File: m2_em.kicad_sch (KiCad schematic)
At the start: 26 parts, among them J15 Bus_M.2_Socket_M, J81 Bus_M.2_Socket_E

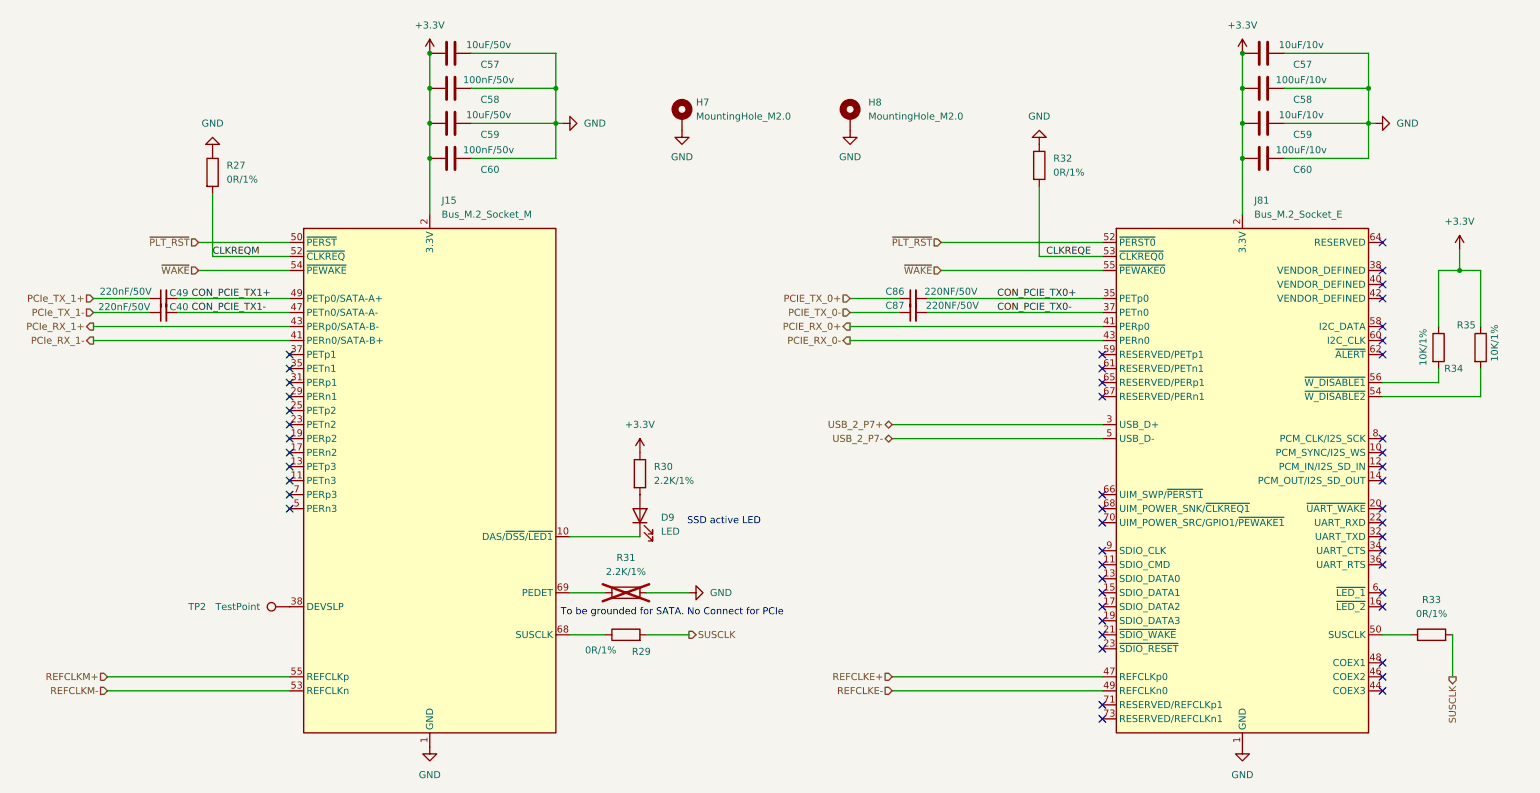
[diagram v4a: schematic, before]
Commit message: Fixed annotation errors duplicate designators on passive components R11 and J15 so that schematic could be imported into pcb. There might be some missing footprints... starting that investigation
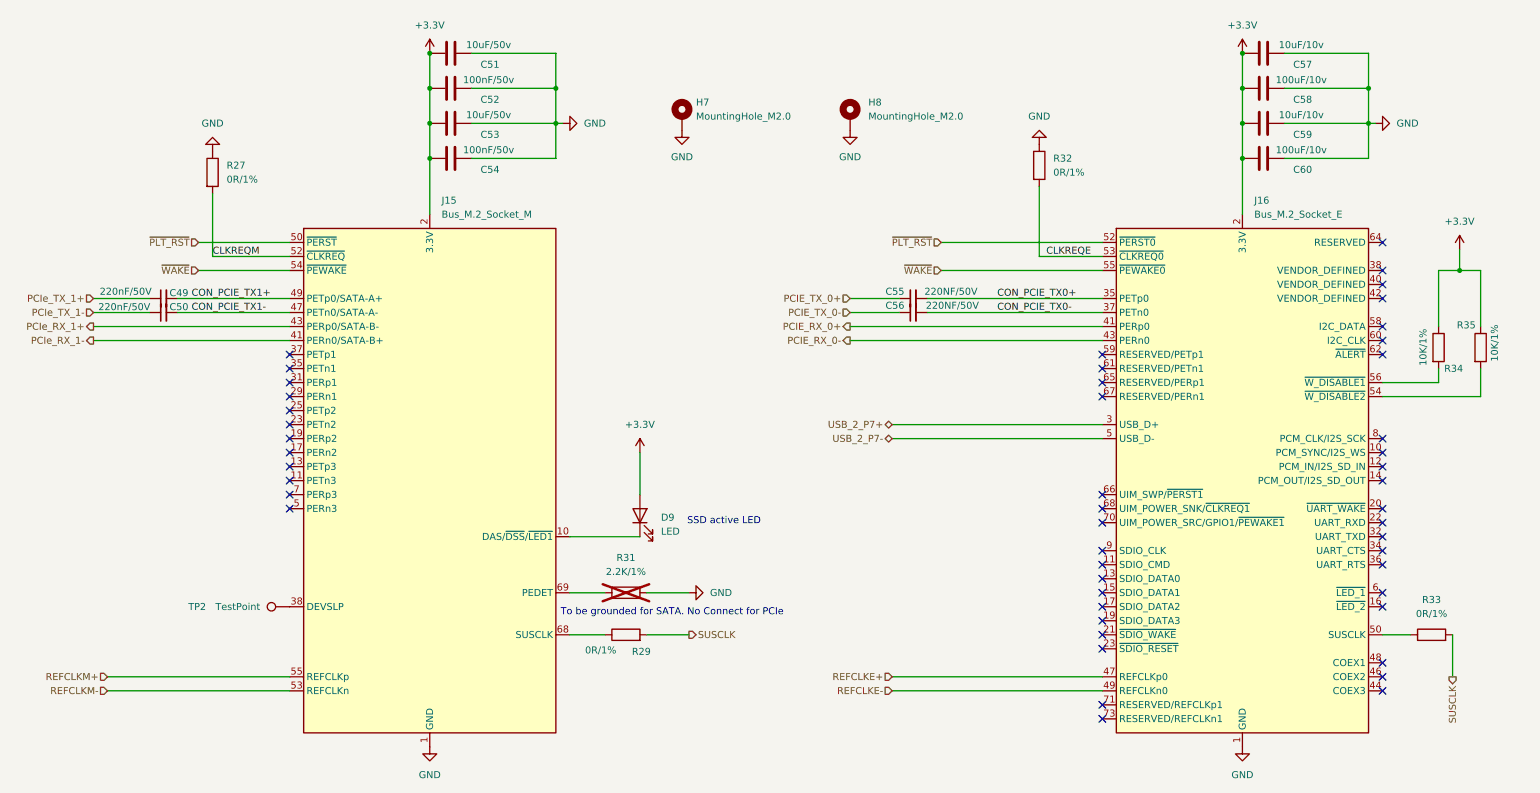
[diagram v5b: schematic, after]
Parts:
- removed R30: 2.2K/1%, A_HDJ_Library:R_0402_1005Metric, symbol Device:R
- renumbered C40 to C50, C57 to C51, C58 to C52, C59 to C53, C60 to C54, C86 to C55, C87 to C56, J81 to J16
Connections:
- net +3.3V: now also D9.2 (A)
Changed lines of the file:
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@@
+	(wire
+		(pts
+			(xy 124.46 102.87) (xy 124.46 110.49)
+		)
+		(stroke
+			(width 0)
+			(type default)
+		)
+	)
 	(wire
 		(pts
@@
 		(in_pos_files yes)
 		(dnp no)
-		(property "Reference" "C40"
+		(property "Reference" "C50"
 			(at 40.894 76.454 90)
 			(show_name no)
@@
 			(project "Carrier_Board"
 				(path "/e768274e-12f3-4f83-96f6-abb7638e0bc1/c9d591b5-2734-4735-842a-ee158b52d7b9"
-					(reference "C40")
+					(reference "C50")
 					(unit 1)
 				)
@@
 	)
 	(symbol
-		(lib_id "Device:R")
-		(at 124.46 106.68 0)
-		(unit 1)
-		(body_style 1)
-		(exclude_from_sim no)
-		(in_bom yes)
-		(on_board yes)
-		(in_pos_files yes)
-		(dnp no)
-		(fields_autoplaced yes)
-		(property "Reference" "R30"
-			(at 127 105.4099 0)
-			(show_name no)
-			(do_not_autoplace no)
-			(effects
-				(font
-					(size 1.27 1.27)
-				)
-				(justify left)
-			)
-		)
-		(property "Value" "2.2K/1%"
-			(at 127 107.9499 0)
-			(show_name no)
-			(do_not_autoplace no)
-			(effects
-				(font
-					(size 1.27 1.27)
-				)
-				(justify left)
-			)
-		)
-		(property "Footprint" "A_HDJ_Library:R_0402_1005Metric"
-			(at 122.682 106.68 90)
-			(hide yes)
-			(show_name no)
-			(do_not_autoplace no)
-			(effects
-				(font
-					(size 1.27 1.27)
-				)
-			)
-		)
-		(property "Datasheet" ""
-			(at 124.46 106.68 0)
-			(hide yes)
-			(show_name no)
-			(do_not_autoplace no)
-			(effects
-				(font
-					(size 1.27 1.27)
-				)
-			)
-		)
-		(property "Description" "Resistor"
-			(at 124.46 106.68 0)
-			(hide yes)
-			(show_name no)
-			(do_not_autoplace no)
-			(effects
-				(font
-					(size 1.27 1.27)
-				)
-			)
-		)
-		(property "Purpose" ""
-			(at 124.46 106.68 0)
-			(show_name no)
-			(do_not_autoplace no)
-			(effects
-				(font
-					(size 1.27 1.27)
-				)
-			)
-		)
-		(pin "1"
-		)
-		(pin "2"
-		)
-		(instances
-			(project "Carrier_Board"
-				(path "/e768274e-12f3-4f83-96f6-abb7638e0bc1/c9d591b5-2734-4735-842a-ee158b52d7b9"
-					(reference "R30")
-					(unit 1)
-				)
-			)
-		)
-	)
-	(symbol
 		(lib_id "Device:C")
 		(at 90.17 36.83 90)
@@
 		(in_pos_files yes)
 		(dnp no)
-		(property "Reference" "C58"
+		(property "Reference" "C52"
 			(at 97.282 38.862 90)
 			(show_name no)
@@
 			(project "Carrier_Board"
 				(path "/e768274e-12f3-4f83-96f6-abb7638e0bc1/c9d591b5-2734-4735-842a-ee158b52d7b9"
-					(reference "C58")
+					(reference "C52")
 					(unit 1)
 				)
@@
 		(in_pos_files yes)
 		(dnp no)
-		(property "Reference" "C87"
+		(property "Reference" "C56"
 			(at 170.688 76.2 90)
 			(show_name no)
@@
 			(project "Carrier_Board"
 				(path "/e768274e-12f3-4f83-96f6-abb7638e0bc1/c9d591b5-2734-4735-842a-ee158b52d7b9"
-					(reference "C87")
+					(reference "C56")
 					(unit 1)
 				)
@@
 		(in_pos_files yes)
 		(dnp no)
-		(property "Reference" "C60"
+		(property "Reference" "C54"
 			(at 97.282 51.562 90)
 			(show_name no)
@@
 			(project "Carrier_Board"
 				(path "/e768274e-12f3-4f83-96f6-abb7638e0bc1/c9d591b5-2734-4735-842a-ee158b52d7b9"
-					(reference "C60")
+					(reference "C54")
 					(unit 1)
 				)
@@
 		(in_pos_files yes)
 		(dnp no)
-		(property "Reference" "C59"
+		(property "Reference" "C53"
 			(at 97.282 45.212 90)
 			(show_name no)
@@
 			(project "Carrier_Board"
 				(path "/e768274e-12f3-4f83-96f6-abb7638e0bc1/c9d591b5-2734-4735-842a-ee158b52d7b9"
-					(reference "C59")
+					(reference "C53")
 					(unit 1)
 				)
@@
 		(dnp no)
 		(fields_autoplaced yes)
-		(property "Reference" "J81"
+		(property "Reference" "J16"
 			(at 235.8233 57.15 0)
 			(show_name no)
@@
 			(project "Carrier_Board"
 				(path "/e768274e-12f3-4f83-96f6-abb7638e0bc1/c9d591b5-2734-4735-842a-ee158b52d7b9"
-					(reference "J81")
+					(reference "J16")
 					(unit 1)
 				)
@@
 		(in_pos_files yes)
 		(dnp no)
-		(property "Reference" "C57"
+		(property "Reference" "C51"
 			(at 97.282 32.512 90)
 			(show_name no)
@@
 			(project "Carrier_Board"
 				(path "/e768274e-12f3-4f83-96f6-abb7638e0bc1/c9d591b5-2734-4735-842a-ee158b52d7b9"
-					(reference "C57")
+					(reference "C51")
 					(unit 1)
 				)
@@
 		(in_pos_files yes)
 		(dnp no)
-		(property "Reference" "C86"
+		(property "Reference" "C55"
 			(at 170.688 73.66 90)
 			(show_name no)
@@
 			(project "Carrier_Board"
 				(path "/e768274e-12f3-4f83-96f6-abb7638e0bc1/c9d591b5-2734-4735-842a-ee158b52d7b9"
-					(reference "C86")
+					(reference "C55")
 					(unit 1)
 				)

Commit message: Updated all the footprints into the pcb editor but all the designator numbers have changed... I have tp go back and fix each one
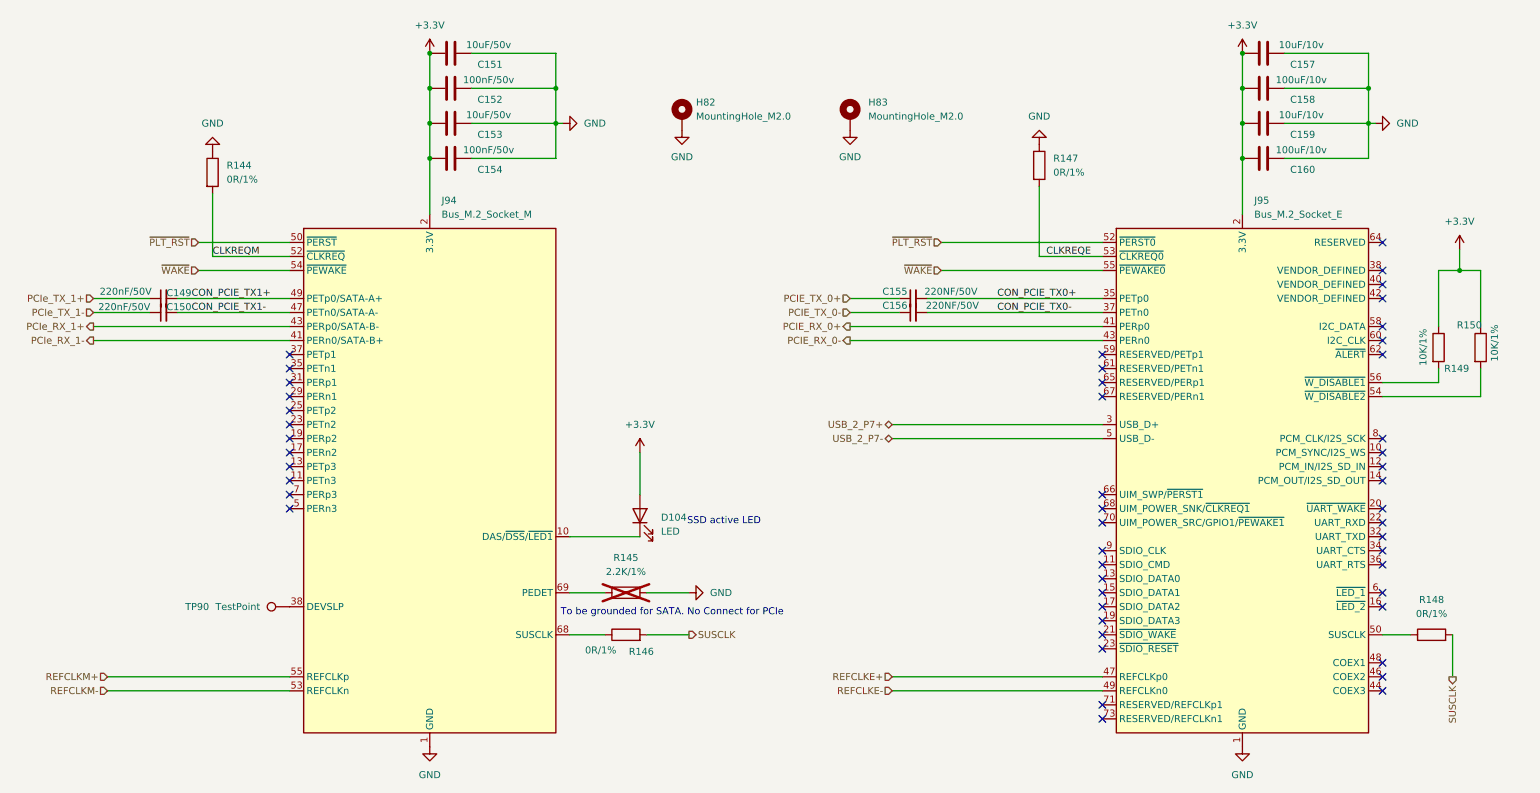
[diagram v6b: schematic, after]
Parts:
- D104: renamed from D9; footprint (none) -> digikey-footprints:LED_0603
- H82: renamed from H7; footprint (none) -> A_HDJ_Library:MountingHole_3.2mm_M3_Pad_Via
- H83: renamed from H8; footprint (none) -> A_HDJ_Library:MountingHole_3.2mm_M3_Pad_Via
- R145: renamed from R31; footprint (none) -> A_HDJ_Library:R_0402_1005Metric
- R150: renamed from R35; footprint (none) -> A_HDJ_Library:R_0402_1005Metric
- TP90: renamed from TP2; footprint (none) -> A_HDJ_Library:TestPoint_Pad_D1.5mm
- renumbered C49 to C149, C50 to C150, C51 to C151, C52 to C152, C53 to C153, C54 to C154, C55 to C155, C56 to C156, C57 to C157, C58 to C158, C59 to C159, C60 to C160, J15 to J94, J16 to J95, R27 to R144, R29 to R146, R32 to R147, R33 to R148, R34 to R149
